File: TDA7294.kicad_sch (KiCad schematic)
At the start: 16 parts, among them J1 PAWER, J2 OUT, J3 IN

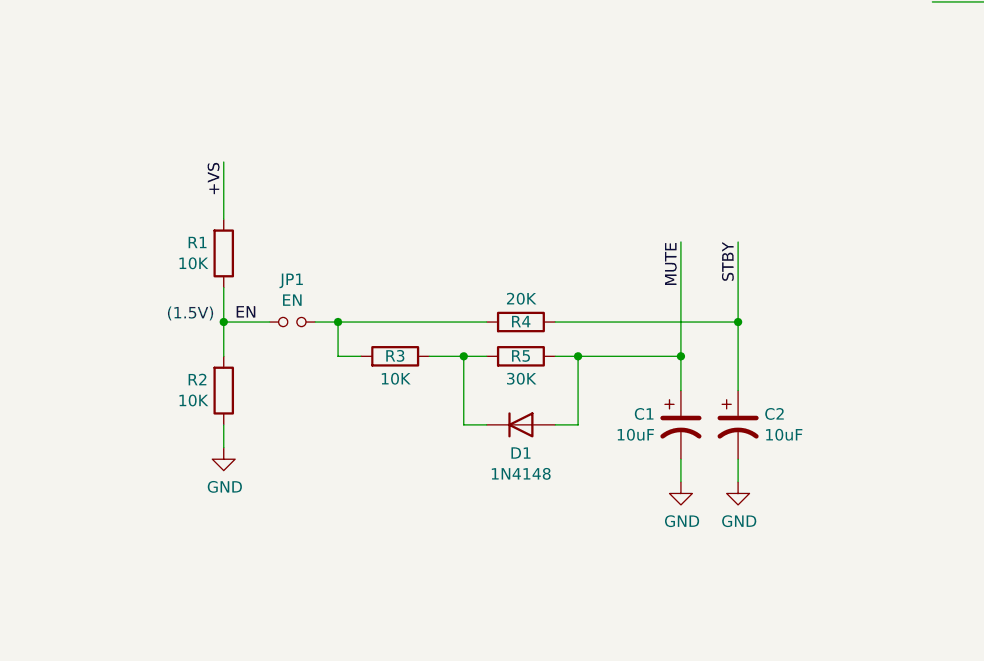
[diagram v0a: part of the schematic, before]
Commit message: eliminando archivos extras
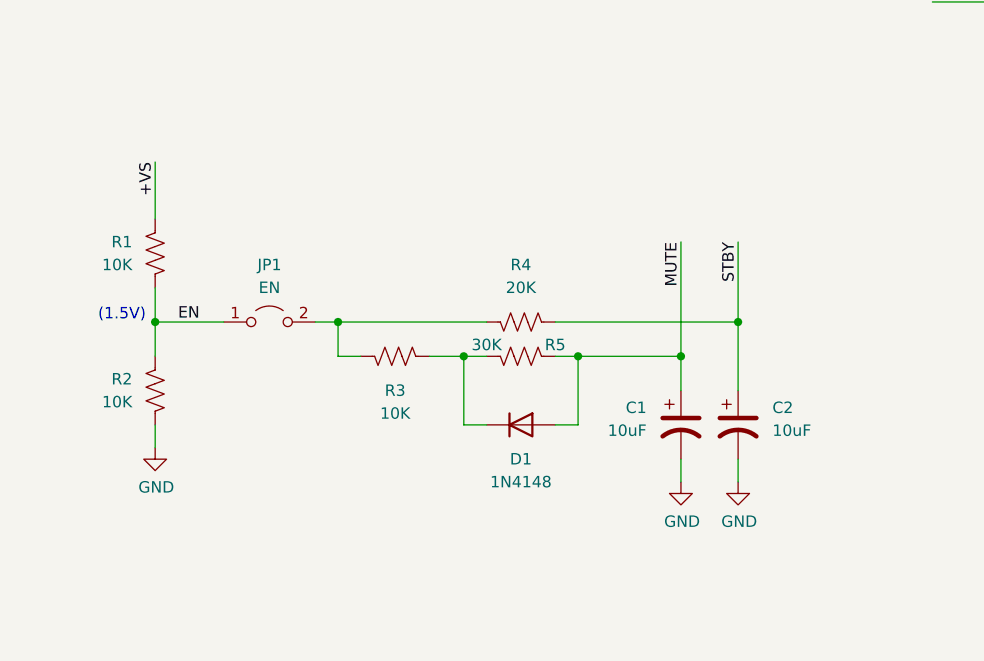
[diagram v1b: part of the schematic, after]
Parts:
- C1, C2: symbol TDA7294-rescue:CP1-Device -> Device:C_Polarized_US
- JP1: symbol TDA7294-rescue:Jumper_NO_Small-Device -> Jumper:Jumper_2_Open
- R1, R2, R3, R4, R5: symbol Device:R -> Device:R_US

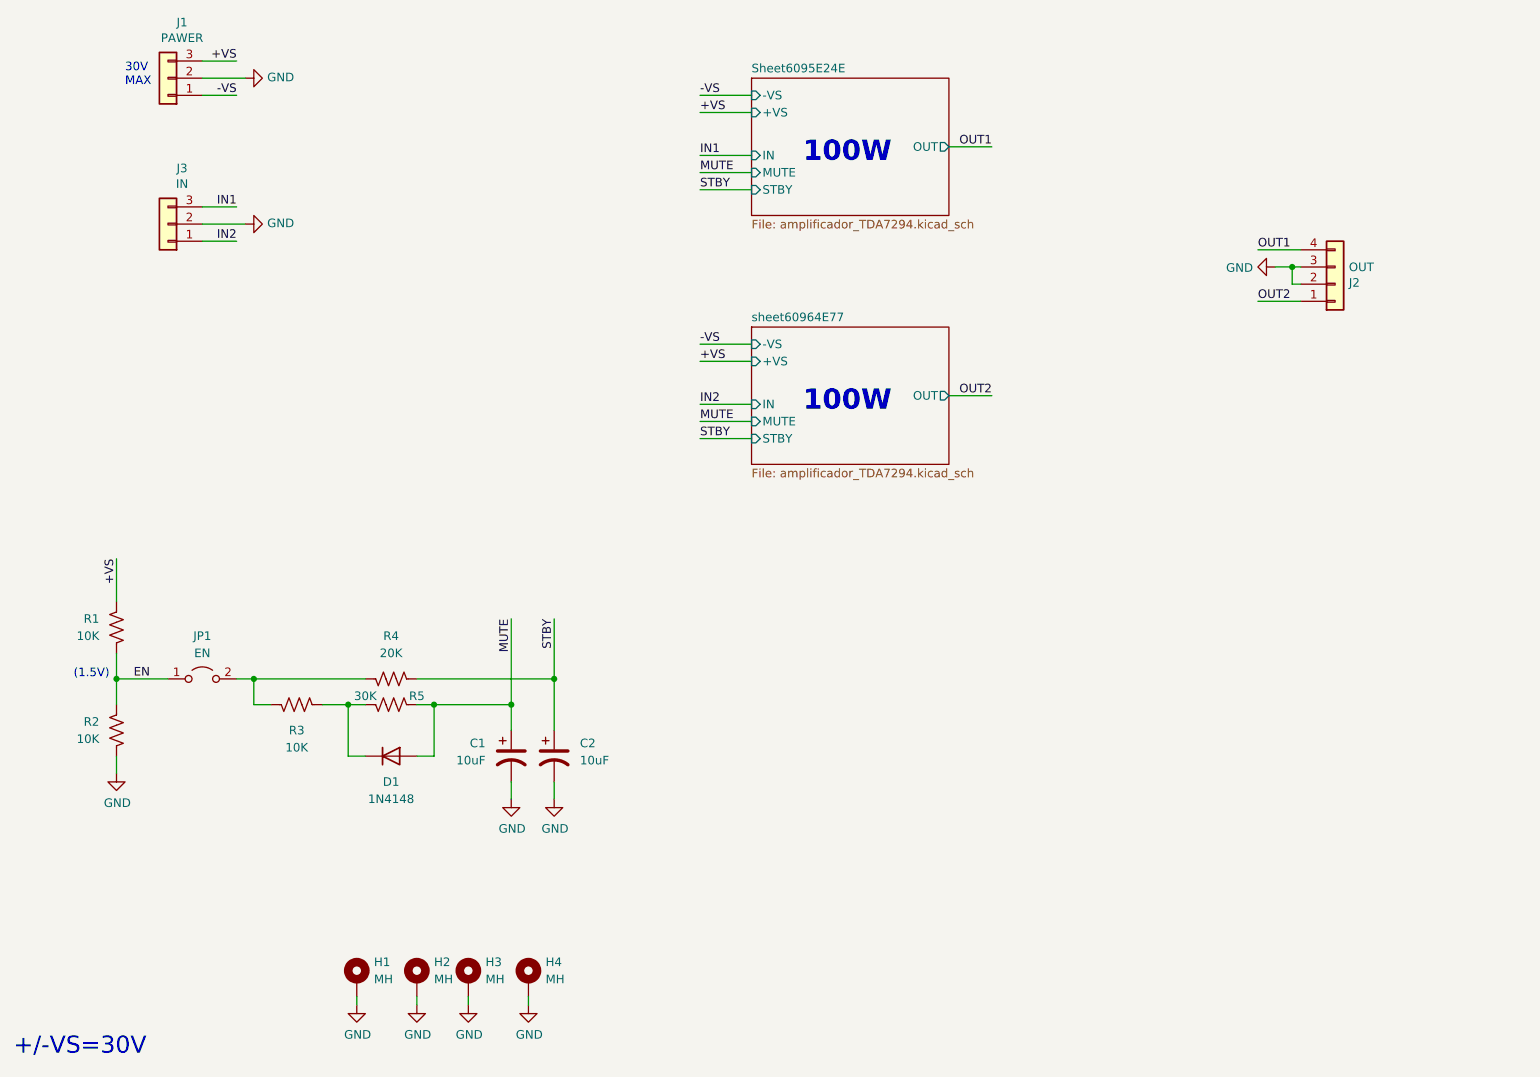
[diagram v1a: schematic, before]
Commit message: completada version 1.1.0 con TDA al mismo lado
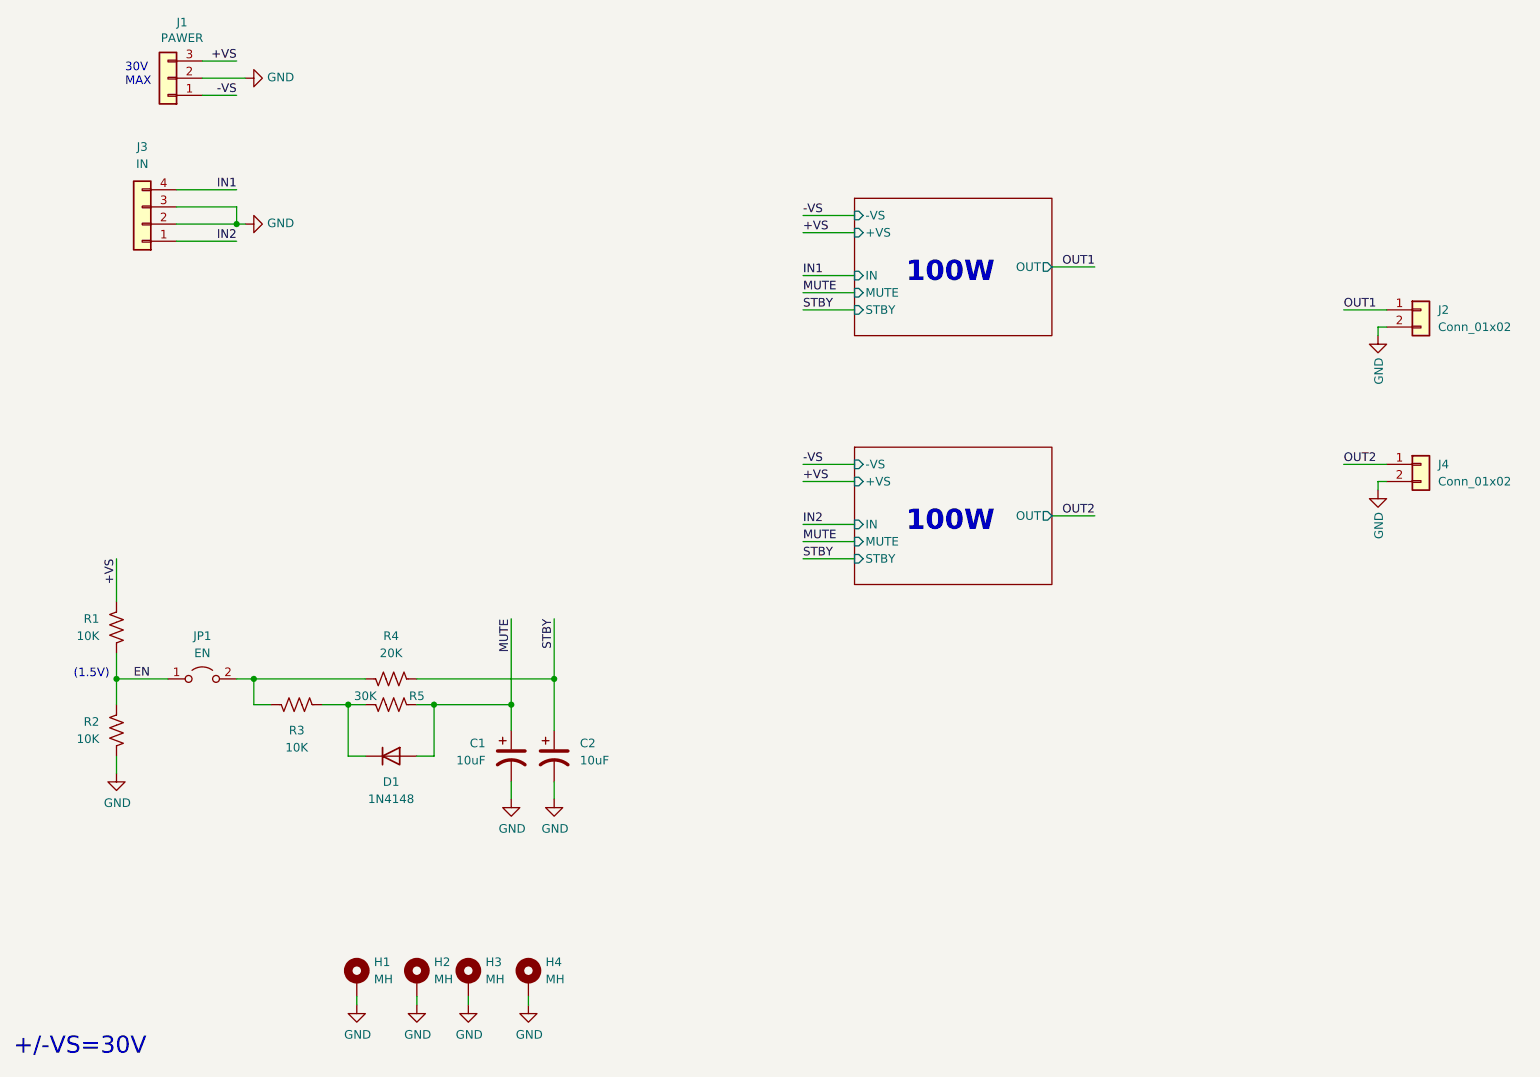
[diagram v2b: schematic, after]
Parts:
- removed J2: OUT, TerminalBlock_Phoenix:TerminalBlock_Phoenix_MKDS-1,5-4-5.08_1x04_P5.08mm_Horizontal, symbol Connector_Generic:Conn_01x04
- added J2, J4: Conn_01x02, Connector_PinHeader_2.54mm:PinHeader_1x02_P2.54mm_Vertical, symbol Connector_Generic:Conn_01x02
- J1: footprint TerminalBlock_Phoenix:TerminalBlock_Phoenix_MKDS-1,5-3-5.08_1x03_P5.08mm_Horizontal -> MR-footprint:TerminalBlock_1x03_P3.50mm_Vertical
- J3: footprint Connector_PinHeader_2.54mm:PinHeader_1x03_P2.54mm_Vertical -> Connector_PinHeader_2.54mm:PinHeader_1x04_P2.54mm_Vertical; symbol Connector_Generic:Conn_01x03 -> Connector_Generic:Conn_01x04
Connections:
- net GND: now also J3.3 (Pin_3), J2.2 (Pin_2), J4.2 (Pin_2)
- net IN1: now also J3.4 (Pin_4); no longer J3.3 (Pin_3)
- net OUT1: now also J2.1 (Pin_1)
- net OUT2: now also J4.1 (Pin_1)

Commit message: mejorando los conectores
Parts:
- H1, H2, H3, H4: now not fitted
- J1: footprint MR-footprint:TerminalBlock_1x03_P3.50mm_Vertical -> Connector_Hirose:Hirose_DF63M-3P-3.96DSA_1x03_P3.96mm_Vertical
- J2, J4: footprint Connector_PinHeader_2.54mm:PinHeader_1x02_P2.54mm_Vertical -> Connector_Molex:Molex_KK-254_AE-6410-02A_1x02_P2.54mm_Vertical
- J3: footprint Connector_PinHeader_2.54mm:PinHeader_1x04_P2.54mm_Vertical -> Connector_Molex:Molex_KK-254_AE-6410-03A_1x03_P2.54mm_Vertical; symbol Connector_Generic:Conn_01x04 -> Connector_Generic:Conn_01x03
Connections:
- net GND: no longer J3.3 (Pin_3)
- net IN1: now also J3.3 (Pin_3); no longer J3.4 (Pin_4)
